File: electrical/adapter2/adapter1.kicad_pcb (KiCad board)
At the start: 2 copper layers, 12 x 49 mm, 7 parts, among them J2 Conn_01x08_Pin

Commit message: start working on adapter2 PCB
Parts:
- added C1: 105, Capacitor_SMD:C_0805_2012Metric_Pad1.18x1.45mm_HandSolder, B.Cu at (103.6, 121.8)
- added C10: 105, Capacitor_SMD:C_0805_2012Metric_Pad1.18x1.45mm_HandSolder, B.Cu at (54.6, 97.1)
- added C11: 105, Capacitor_SMD:C_0805_2012Metric_Pad1.18x1.45mm_HandSolder, B.Cu at (54.6, 100.1)
- added C12: 105, Capacitor_SMD:C_0805_2012Metric_Pad1.18x1.45mm_HandSolder, B.Cu at (54.6, 103.2)
- added C15: 104 !, Capacitor_SMD:C_0805_2012Metric_Pad1.18x1.45mm_HandSolder, B.Cu at (54.6, 106.2)
- added C2: 105, Capacitor_SMD:C_0805_2012Metric_Pad1.18x1.45mm_HandSolder, B.Cu at (64.2, 97.1)
- added C3: 104 !, Capacitor_SMD:C_0805_2012Metric_Pad1.18x1.45mm_HandSolder, B.Cu at (64.2, 100.1)
- added C4: 4.7uF/50V, Capacitor_SMD:C_0805_2012Metric_Pad1.18x1.45mm_HandSolder, B.Cu at (64.2, 103.2)
- added C5: 105, Capacitor_SMD:C_0805_2012Metric_Pad1.18x1.45mm_HandSolder, B.Cu at (64.2, 106.2)
- added C6: 4.7uF/50V, Capacitor_SMD:C_0805_2012Metric_Pad1.18x1.45mm_HandSolder, B.Cu at (59.4, 97.1)
- added C7: 105, Capacitor_SMD:C_0805_2012Metric_Pad1.18x1.45mm_HandSolder, B.Cu at (59.4, 100.1)
- added C8: 105, Capacitor_SMD:C_0805_2012Metric_Pad1.18x1.45mm_HandSolder, B.Cu at (59.4, 103.2)
- added C9: 105, Capacitor_SMD:C_0805_2012Metric_Pad1.18x1.45mm_HandSolder, B.Cu at (59.4, 106.2)
- added D1: MBR0530, Diode_SMD:D_SOD-123, B.Cu at (42.7, 97.3)
- added D2: MBR0530, Diode_SMD:D_SOD-123, B.Cu at (42.7, 100.7)
- added D3: MBR0530, Diode_SMD:D_SOD-123, B.Cu at (42.7, 104.0)
- added J3: 0.5 mm, 24P, Connector_FFC-FPC:Jushuo_AFC07-S24FCA-00_1x24-1MP_P0.50_Horizontal, B.Cu at (108.6, 126.0)
- added J4: 0.5 mm, 24P, Connector_FFC-FPC:Jushuo_AFC07-S24FCA-00_1x24-1MP_P0.50_Horizontal, F.Cu at (108.6, 126.0)
- added JP3: SolderJumper_3_Bridged12, Jumper:SolderJumper-3_P1.3mm_Bridged12_RoundedPad1.0x1.5mm, B.Cu at (60.0, 85.2)
- added JP4: SolderJumper_2_Open, Jumper:SolderJumper-2_P1.3mm_Open_TrianglePad1.0x1.5mm, B.Cu at (50.0, 105.7)
- added Q1: BSS138, Package_TO_SOT_SMD:SOT-23, B.Cu at (39.7, 71.0)
- added Q2: AO3401A, Package_TO_SOT_SMD:SOT-23, B.Cu at (39.7, 75.6)
- added Q3: S8050 SMD, Package_TO_SOT_SMD:SOT-23, B.Cu at (50.2, 98.9)
- added R10: DNP, Resistor_SMD:R_0603_1608Metric_Pad0.98x0.95mm_HandSolder, B.Cu at (50.0, 102.7)
- added R2: 10k, Resistor_SMD:R_0805_2012Metric_Pad1.20x1.40mm_HandSolder, B.Cu at (39.8, 79.3)
- added R3: 100k, Resistor_SMD:R_0805_2012Metric_Pad1.20x1.40mm_HandSolder, B.Cu at (39.8, 82.2)
- added R5: 10k, Resistor_SMD:R_0805_2012Metric_Pad1.20x1.40mm_HandSolder, B.Cu at (39.8, 85.2)
- added R6: 1k, Resistor_SMD:R_0805_2012Metric_Pad1.20x1.40mm_HandSolder, B.Cu at (39.8, 88.1)
- added R7: 47k, Resistor_SMD:R_0805_2012Metric_Pad1.20x1.40mm_HandSolder, B.Cu at (39.8, 91.1)
- added R8: 47k, Resistor_SMD:R_0805_2012Metric_Pad1.20x1.40mm_HandSolder, B.Cu at (39.8, 94.0)
- added U1: ~, fw16_epaper:RP2040-Tiny, B.Cu at (125.5, 102.2)
- J2: moved to F.Cu
- R1: value DNP -> 0.47R; footprint Resistor_SMD:R_0603_1608Metric_Pad0.98x0.95mm_HandSolder -> Resistor_SMD:R_0805_2012Metric_Pad1.20x1.40mm_HandSolder
- moved J2 4.00 mm to (125.5, 91.2), turned to 0 degrees
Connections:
- R1 pad 1: Net-(J1-BOARD_ID) -> GND
- R1 pad 2: GND -> Net-(Q1-S)
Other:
- board size 12 x 49 mm -> 12 x 53 mm
- board text added: "1"
- board text added: "24"

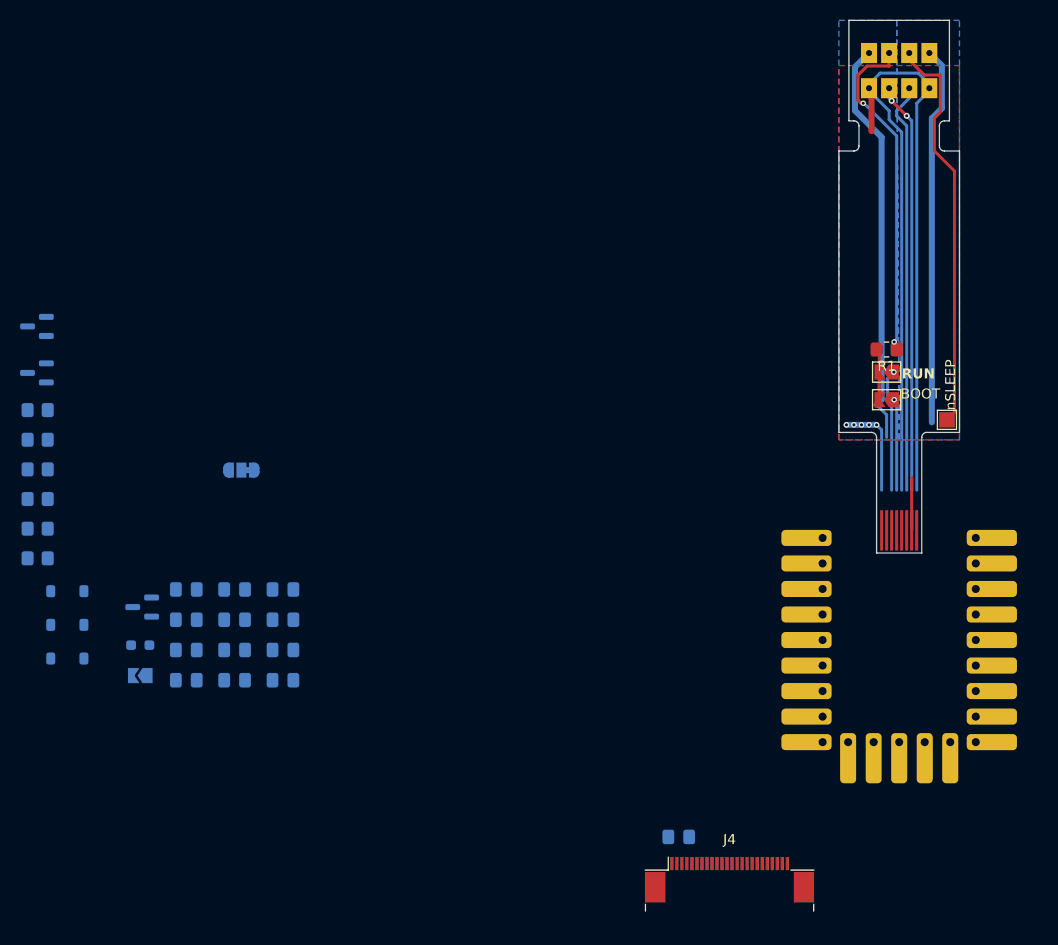
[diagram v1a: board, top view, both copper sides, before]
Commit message: adapter2: routing done and DRC clean
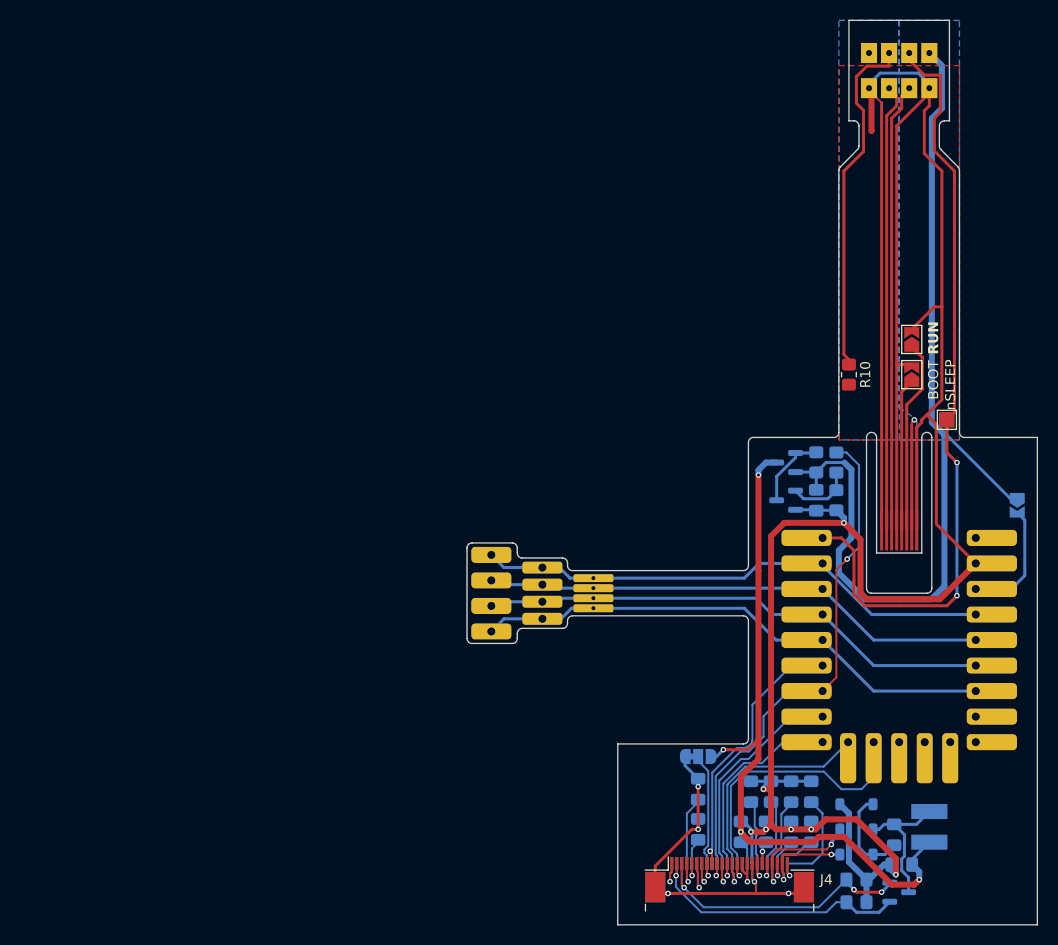
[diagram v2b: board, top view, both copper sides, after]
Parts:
- removed R6: 1k, Resistor_SMD:R_0805_2012Metric_Pad1.20x1.40mm_HandSolder
- removed R8: 47k, Resistor_SMD:R_0805_2012Metric_Pad1.20x1.40mm_HandSolder
- added J5: ~, fw16_epaper:TouchConnector, B.Cu at (84.9, 97.5)
- added L1: 68uH, Inductor_SMD:L_Bourns-SRN4018, B.Cu at (128.5, 120.8)
- R1: moved to B.Cu
- R10: footprint Resistor_SMD:R_0603_1608Metric_Pad0.98x0.95mm_HandSolder -> Resistor_SMD:R_0805_2012Metric_Pad1.20x1.40mm_HandSolder; moved to F.Cu
- moved Q1 102.6 mm to (125.5, 127.2), turned to 0 degrees
- moved R2 95.1 mm to (121.2, 128.2)
- moved JP4 88.9 mm to (137.2, 88.8), turned to -90 degrees
- moved D2 81.8 mm to (121.2, 123.5)
- moved D1 81.3 mm to (121.2, 118.5), turned to 0 degrees
- moved D3 80.3 mm to (121.2, 121.0), turned to 0 degrees
- moved R7 79.5 mm to (119.2, 88.2), turned to 90 degrees
- moved R5 79.5 mm to (119.2, 84.5), turned to 90 degrees
- moved R3 77.5 mm to (117.2, 84.5), turned to -90 degrees
- moved R10 75.5 mm to (120.5, 75.8), turned to -90 degrees
- moved Q2 75.1 mm to (114.2, 84.5)
- moved C6 70.0 mm to (125.0, 121.5), turned to 90 degrees
- moved C11 65.7 mm to (116.8, 121.2), turned to -90 degrees
- moved C15 65.2 mm to (117.2, 88.2), turned to 90 degrees
- moved C4 65.2 mm to (125.8, 124.5), turned to 0 degrees
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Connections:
- C4 pad 2: +3V3 -> /3V3_EP
- J4 pad MP: unconnected-(J4-MountPin-PadMP) -> GND
- Q1 pad 1: Net-(Q1-G) -> /GDR
- Q1 pad 2: Net-(Q1-S) -> /RESE
- R1 pad 2: Net-(Q1-S) -> /RESE
- R2 pad 2: Net-(Q1-G) -> /GDR
- U1 pad 1: unconnected-(U1-Pad1) -> Net-(J5-Pin_1)
- U1 pad 10: unconnected-(U1-Pad10) -> /DIN
- U1 pad 14: /BUSY -> unconnected-(U1-Pad14)
- U1 pad 15: /RST -> unconnected-(U1-Pad15)
- U1 pad 16: /SCK -> Net-(J5-Pin_4)
- U1 pad 17: /DIN -> Net-(J5-Pin_3)
- U1 pad 18: /DC -> Net-(J5-Pin_2)
- U1 pad 19: /CS -> Net-(J5-Pin_1)
- U1 pad 2: unconnected-(U1-Pad2) -> Net-(J5-Pin_2)
- U1 pad 3: unconnected-(U1-Pad3) -> Net-(J5-Pin_3)
- U1 pad 4: unconnected-(U1-Pad4) -> Net-(J5-Pin_4)
- U1 pad 5: unconnected-(U1-Pad5) -> /BUSY
- U1 pad 6: unconnected-(U1-Pad6) -> /RST
- U1 pad 7: unconnected-(U1-Pad7) -> /DC
- U1 pad 8: unconnected-(U1-Pad8) -> /CS
- U1 pad 9: unconnected-(U1-Pad9) -> /SCK
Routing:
- net GND: track 108.7 -> 322.0 mm, vias 5 -> 12
- net /3V3_EP: track 0.00 -> 79.2 mm, vias 0 -> 5
- net +3V3: track 37.7 -> 96.6 mm
- net /RST: track 0.00 -> 53.3 mm, vias 0 -> 2
- net Net-(J5-Pin_4): track 0.00 -> 52.6 mm
- net Net-(J5-Pin_1): track 0.00 -> 52.0 mm
- net Net-(J5-Pin_3): track 0.00 -> 51.3 mm
- net Net-(J5-Pin_2): track 0.00 -> 50.7 mm
- net /SLEEP: track 40.1 -> 77.2 mm, vias 0 -> 2
- net +5V: track 45.8 -> 11.1 mm, vias 0 -> 1
- net /DIN: track 0.00 -> 30.1 mm, vias 0 -> 1
- net /RESE: track 0.00 -> 28.5 mm, vias 0 -> 3
- net /BUSY: track 0.00 -> 28.0 mm, vias 0 -> 1
- net /GDR: track 0.00 -> 27.2 mm, vias 0 -> 1
- net /SCK: track 0.00 -> 25.6 mm, vias 0 -> 1
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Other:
- board size 12 x 53 mm -> 56.8 x 90 mm
- board text added: "3wire"
- board text added: "4wire"
